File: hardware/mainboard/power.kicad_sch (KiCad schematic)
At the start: 18 parts, among them J1 Eurorack Power, U1 LD1117-3.3, U2 LM4040DBZ-10

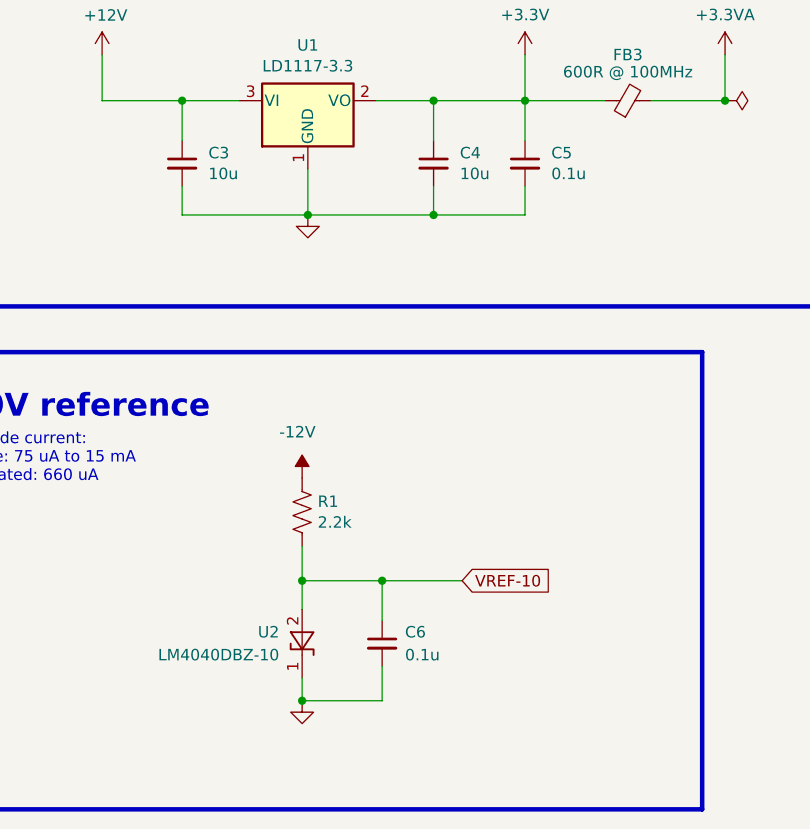
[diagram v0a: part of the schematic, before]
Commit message: Switch audio filter caps to 0603. Start auditing BOM
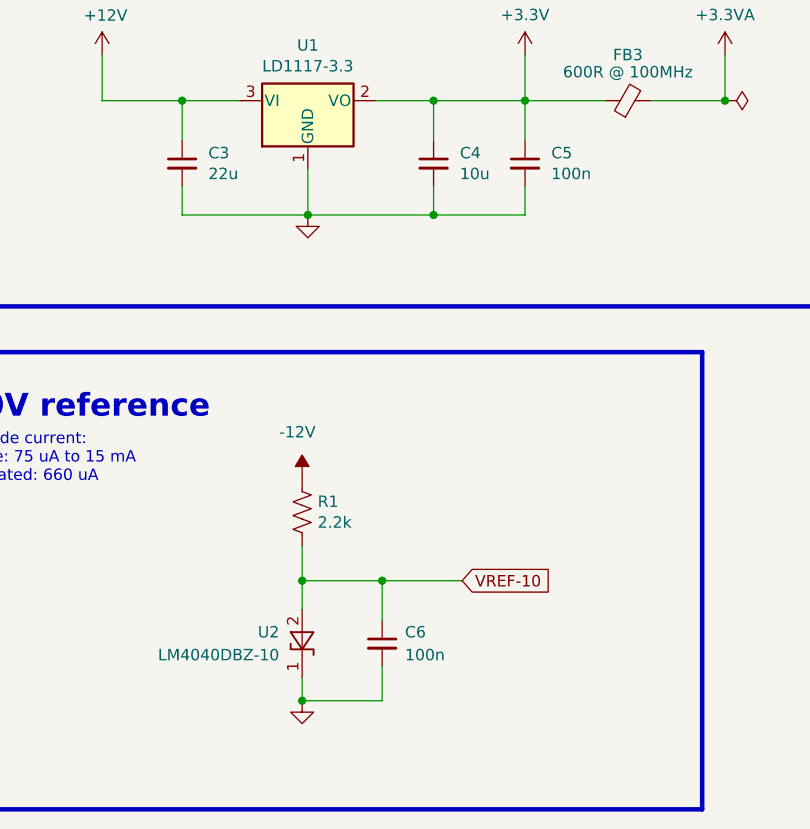
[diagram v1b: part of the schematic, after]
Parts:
- C1: Reqs power bypass, 16V+ -> Bulk capacitance, 16 V
- C2: Reqs power bypass, 16V+ -> Board bulk capacitance, 16 V
- C3: value 10u -> 22u; Reqs ESR 0.3-22 Ohms, 16v+ -> Linear regulator input filter, 16 V
- C4: footprint Capacitor_SMD:C_0805_2012Metric_Pad1.18x1.45mm_HandSolder -> Capacitor_SMD:C_0603_1608Metric_Pad1.08x0.95mm_HandSolder; Reqs (none) -> Linear regulator output filter, 10 V; mpn (none) -> CL10A106MP8NNNC
- C5, C6: value 0.1u -> 100n; Reqs bypass, 16v+ -> Bypass, 16 V; finalized yes -> (none); mpn MF-CAP-0603-0.1uF -> (none); mpn alt GCM188R91E104KA37D -> (none); mpn specs 10%, 25v -> (none)
- D1, D2: Reqs Schottky, 1A -> (none); finalized yes -> (none)
- FB1, FB2: Reqs >500mA DC current -> Power filter, 500mA DC current; finalized yes -> (none)
- FB3: Reqs >200mA DC current -> Analog power filter, 200mA DC current; finalized yes -> (none)
- R1: Reqs 1%, 60mW, vref current control -> -10V zener current control, 1%, 60 mW; mpn alt ERA-3AED222V -> (none); mpn specs 125mW, 1% -> (none)
- TP1, TP2, TP3: finalized yes -> n/a
- U1: finalized no -> (none); mpn AZ1117CD-3.3TRG1, LD1117DT33TR -> LD1117DT33TR, AZ1117CD-3.3TRG1
- U2: finalized yes -> (none)
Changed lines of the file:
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@@
       (effects (font (size 1.27 1.27)) hide)
     )
-    (property "finalized" "yes" (id 4) (at 80.645 41.275 0)
+    (property "finalized" "" (id 4) (at 80.645 41.275 0)
       (effects (font (size 1.27 1.27)) hide)
     )
@@
       (effects (font (size 1.27 1.27)) hide)
     )
-    (property "Reqs" "Schottky, 1A" (id 7) (at 80.645 41.275 0)
+    (property "Reqs" "" (id 7) (at 80.645 41.275 0)
       (effects (font (size 1.27 1.27)) hide)
     )
@@
       (effects (font (size 1.27 1.27)) hide)
     )
-    (property "finalized" "yes" (id 4) (at 80.645 37.465 0)
+    (property "finalized" "" (id 4) (at 80.645 37.465 0)
       (effects (font (size 1.27 1.27)) hide)
     )
@@
       (effects (font (size 1.27 1.27)) hide)
     )
-    (property "Reqs" "Schottky, 1A" (id 7) (at 80.645 37.465 0)
+    (property "Reqs" "" (id 7) (at 80.645 37.465 0)
       (effects (font (size 1.27 1.27)) hide)
     )
@@
       (effects (font (size 1.27 1.27)) hide)
     )
-    (property "finalized" "no" (id 4) (at 60.325 109.22 0)
-      (effects (font (size 1.27 1.27)) hide)
-    )
-    (property "mpn" "AZ1117CD-3.3TRG1, LD1117DT33TR" (id 5) (at 60.325 109.22 0)
+    (property "finalized" "" (id 4) (at 60.325 109.22 0)
+      (effects (font (size 1.27 1.27)) hide)
+    )
+    (property "mpn" "LD1117DT33TR, AZ1117CD-3.3TRG1" (id 5) (at 60.325 109.22 0)
       (effects (font (size 1.27 1.27)) hide)
     )
@@
       (effects (font (size 1.27 1.27)) (justify left))
     )
-    (property "Value" "10u" (id 1) (at 49.276 117.348 0)
+    (property "Value" "22u" (id 1) (at 49.276 117.348 0)
       (effects (font (size 1.27 1.27)) (justify left))
     )
@@
       (effects (font (size 1.27 1.27)) hide)
     )
-    (property "Reqs" "ESR 0.3-22 Ohms, 16v+" (id 6) (at 46.355 116.205 0)
+    (property "Reqs" "Linear regulator input filter, 16 V" (id 6) (at 46.355 116.205 0)
       (effects (font (size 1.27 1.27)) hide)
     )
@@
       (effects (font (size 1.27 1.27)) (justify left))
     )
-    (property "Footprint" "Capacitor_SMD:C_0805_2012Metric_Pad1.18x1.45mm_HandSolder" (id 2) (at 74.295 116.205 0)
+    (property "Footprint" "Capacitor_SMD:C_0603_1608Metric_Pad1.08x0.95mm_HandSolder" (id 2) (at 74.295 116.205 0)
       (effects (font (size 1.27 1.27)) hide)
     )
@@
       (effects (font (size 1.27 1.27)) hide)
     )
-    (property "Reqs" "" (id 4) (at 74.295 116.205 0)
-      (effects (font (size 1.27 1.27)) hide)
-    )
-    (property "mpn" "" (id 5) (at 74.295 116.205 0)
+    (property "Reqs" "Linear regulator output filter, 10 V" (id 4) (at 74.295 116.205 0)
+      (effects (font (size 1.27 1.27)) hide)
+    )
+    (property "mpn" "CL10A106MP8NNNC" (id 5) (at 74.295 116.205 0)
       (effects (font (size 1.27 1.27)) hide)
     )
@@
       (effects (font (size 1.27 1.27)) (justify left))
     )
-    (property "Value" "0.1u" (id 1) (at 87.376 117.348 0)
+    (property "Value" "100n" (id 1) (at 87.376 117.348 0)
       (effects (font (size 1.27 1.27)) (justify left))
     )
@@
       (effects (font (size 1.27 1.27)) hide)
     )
-    (property "finalized" "yes" (id 4) (at 84.455 116.205 0)
-      (effects (font (size 1.27 1.27)) hide)
-    )
-    (property "mpn" "MF-CAP-0603-0.1uF" (id 5) (at 84.455 116.205 0)
-      (effects (font (size 1.27 1.27)) hide)
-    )
-    (property "mpn specs" "10%, 25v" (id 6) (at 84.455 116.205 0)
-      (effects (font (size 1.27 1.27)) hide)
-    )
-    (property "mpn alt" "GCM188R91E104KA37D" (id 7) (at 84.455 116.205 0)
-      (effects (font (size 1.27 1.27)) hide)
-    )
-    (property "Reqs" "bypass, 16v+" (id 8) (at 84.455 116.205 0)
+    (property "finalized" "" (id 4) (at 84.455 116.205 0)
+      (effects (font (size 1.27 1.27)) hide)
+    )
+    (property "mpn" "" (id 5) (at 84.455 116.205 0)
+      (effects (font (size 1.27 1.27)) hide)
+    )
+    (property "mpn specs" "" (id 6) (at 84.455 116.205 0)
+      (effects (font (size 1.27 1.27)) hide)
+    )
+    (property "mpn alt" "" (id 7) (at 84.455 116.205 0)
+      (effects (font (size 1.27 1.27)) hide)
+    )
+    (property "Reqs" "Bypass, 16 V" (id 8) (at 84.455 116.205 0)
       (effects (font (size 1.27 1.27)) hide)
     )
@@
       (effects (font (size 1.27 1.27)) hide)
     )
-    (property "finalized" "yes" (id 5) (at 95.885 109.22 0)
+    (property "finalized" "" (id 5) (at 95.885 109.22 0)
       (effects (font (size 1.27 1.27)) hide)
     )
@@
       (effects (font (size 1.27 1.27)) hide)
     )
-    (property "Reqs" ">200mA DC current" (id 7) (at 95.885 109.22 0)
+    (property "Reqs" "Analog power filter, 200mA DC current" (id 7) (at 95.885 109.22 0)
       (effects (font (size 1.27 1.27)) hide)
     )
@@
       (effects (font (size 1.27 1.27)) hide)
     )
-    (property "finalized" "yes" (id 5) (at 62.23 41.275 0)
+    (property "finalized" "" (id 5) (at 62.23 41.275 0)
       (effects (font (size 1.27 1.27)) hide)
     )
@@
       (effects (font (size 1.27 1.27)) hide)
     )
-    (property "Reqs" ">500mA DC current" (id 7) (at 62.23 41.275 0)
+    (property "Reqs" "Power filter, 500mA DC current" (id 7) (at 62.23 41.275 0)
       (effects (font (size 1.27 1.27)) hide)
     )
@@
       (effects (font (size 1.27 1.27)) hide)
     )
-    (property "finalized" "yes" (id 5) (at 62.23 37.465 0)
+    (property "finalized" "" (id 5) (at 62.23 37.465 0)
       (effects (font (size 1.27 1.27)) hide)
     )
@@
       (effects (font (size 1.27 1.27)) hide)
     )
-    (property "Reqs" ">500mA DC current" (id 7) (at 62.23 37.465 0)
+    (property "Reqs" "Power filter, 500mA DC current" (id 7) (at 62.23 37.465 0)
       (effects (font (size 1.27 1.27)) hide)
     )
@@
       (effects (font (size 1.27 1.27) italic) hide)
     )
-    (property "finalized" "yes" (id 4) (at 59.69 169.545 0)
+    (property "finalized" "" (id 4) (at 59.69 169.545 0)
       (effects (font (size 1.27 1.27)) hide)
     )
@@
       (effects (font (size 1.27 1.27)) hide)
     )
-    (property "Reqs" "1%, 60mW, vref current control" (id 6) (at 59.69 154.94 0)
-      (effects (font (size 1.27 1.27)) hide)
-    )
-    (property "mpn specs" "125mW,  1%" (id 7) (at 59.69 154.94 0)
-      (effects (font (size 1.27 1.27)) hide)
-    )
-    (property "mpn alt" "ERA-3AED222V" (id 8) (at 59.69 154.94 0)
+    (property "Reqs" "-10V zener current control, 1%, 60 mW" (id 6) (at 59.69 154.94 0)
+      (effects (font (size 1.27 1.27)) hide)
+    )
+    (property "mpn specs" "" (id 7) (at 59.69 154.94 0)
+      (effects (font (size 1.27 1.27)) hide)
+    )
+    (property "mpn alt" "" (id 8) (at 59.69 154.94 0)
       (effects (font (size 1.27 1.27)) hide)
     )
@@
       (effects (font (size 1.27 1.27)) (justify left))
     )
-    (property "Value" "0.1u" (id 1) (at 71.12 170.815 0)
+    (property "Value" "100n" (id 1) (at 71.12 170.815 0)
       (effects (font (size 1.27 1.27)) (justify left))
     )
@@
       (effects (font (size 1.27 1.27)) hide)
     )
-    (property "finalized" "yes" (id 4) (at 68.58 169.545 0)
-      (effects (font (size 1.27 1.27)) hide)
-    )
-    (property "mpn" "MF-CAP-0603-0.1uF" (id 5) (at 68.58 169.545 0)
-      (effects (font (size 1.27 1.27)) hide)
-    )
-    (property "mpn specs" "10%, 25v" (id 6) (at 68.58 169.545 0)
-      (effects (font (size 1.27 1.27)) hide)
-    )
-    (property "mpn alt" "GCM188R91E104KA37D" (id 7) (at 68.58 169.545 0)
-      (effects (font (size 1.27 1.27)) hide)
-    )
-    (property "Reqs" "bypass, 16v+" (id 8) (at 68.58 169.545 0)
+    (property "finalized" "" (id 4) (at 68.58 169.545 0)
+      (effects (font (size 1.27 1.27)) hide)
+    )
+    (property "mpn" "" (id 5) (at 68.58 169.545 0)
+      (effects (font (size 1.27 1.27)) hide)
+    )
+    (property "mpn specs" "" (id 6) (at 68.58 169.545 0)
+      (effects (font (size 1.27 1.27)) hide)
+    )
+    (property "mpn alt" "" (id 7) (at 68.58 169.545 0)
+      (effects (font (size 1.27 1.27)) hide)
+    )
+    (property "Reqs" "Bypass, 16 V" (id 8) (at 68.58 169.545 0)
       (effects (font (size 1.27 1.27)) hide)
     )
@@
       (effects (font (size 1.27 1.27)) hide)
     )
-    (property "Reqs" "power bypass, 16V+" (id 7) (at 88.265 52.07 0)
+    (property "Reqs" "Bulk capacitance, 16 V" (id 7) (at 88.265 52.07 0)
       (effects (font (size 1.27 1.27)) hide)
     )
@@
       (effects (font (size 1.27 1.27)) hide)
     )
-    (property "finalized" "yes" (id 5) (at 234.95 146.685 0)
+    (property "finalized" "n/a" (id 5) (at 234.95 146.685 0)
       (effects (font (size 1.27 1.27)) hide)
     )
@@
       (effects (font (size 1.27 1.27)) hide)
     )
-    (property "finalized" "yes" (id 5) (at 234.95 135.255 0)
+    (property "finalized" "n/a" (id 5) (at 234.95 135.255 0)
       (effects (font (size 1.27 1.27)) hide)
     )
@@
       (effects (font (size 1.27 1.27)) hide)
     )
-    (property "Reqs" "power bypass, 16V+" (id 7) (at 99.06 52.07 0)
+    (property "Reqs" "Board bulk capacitance, 16 V" (id 7) (at 99.06 52.07 0)
       (effects (font (size 1.27 1.27)) hide)
     )
@@
       (effects (font (size 1.27 1.27)) hide)
     )
-    (property "finalized" "yes" (id 5) (at 234.95 140.97 0)
-      (effects (font (size 1.27 1.27)) hide)
-    )
+    (property "finalized" "n/a" (id 5) (at 234.95 140.97 0)
+      (effects (font (size 1.27 1.27)) hide)
+    )

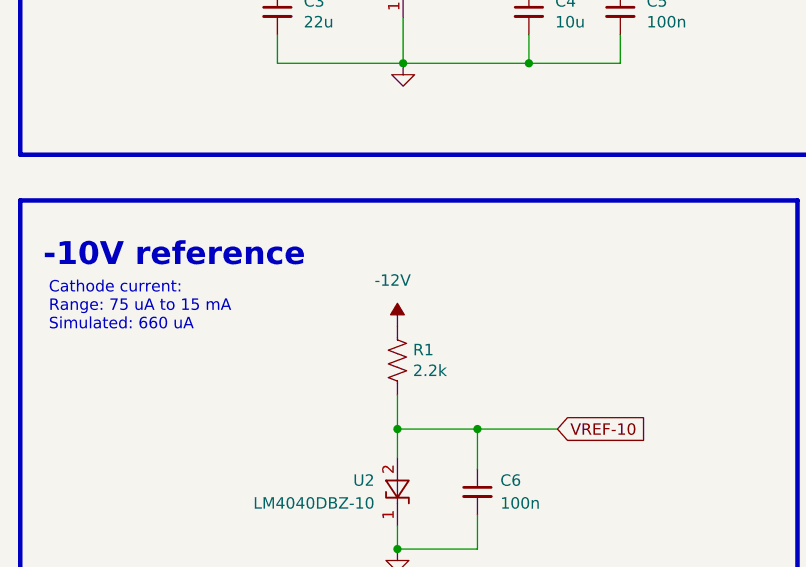
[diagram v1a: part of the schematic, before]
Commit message: Audit BOM, replace some parts with alts
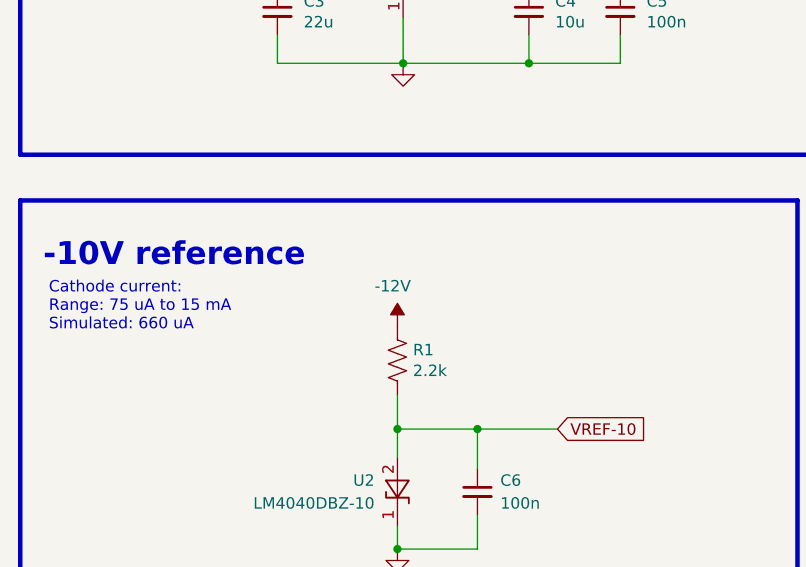
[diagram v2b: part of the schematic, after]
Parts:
- C1, C2, C3: finalized (none) -> yes; mpn (none) -> CL21A226MAYNNNE
- C4, FB1, FB2, FB3, U2: finalized (none) -> yes
- C5, C6: finalized (none) -> yes; macrofab_mpn (none) -> MF-CAP-0402-0.1uF; mpn (none) -> CL05B104KO5NNNC
- D1, D2: finalized (none) -> yes; mpn B0520LWQ-7-F -> PMEG2005EGWJ, PMEG3005EGWX
- J1: finalized (none) -> yes; mpn 302-S101 -> 4UCONN 20253, On-shore 302-S101
- R1: Reqs -10V zener current control, 1%, 60 mW -> -10V zener current control, 1%, 100 mW, thick film; macrofab_mpn (none) -> MF-RES-0402-2K
- U1: finalized (none) -> needs testing
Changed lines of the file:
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@@
       (effects (font (size 1.27 1.27)) hide)
     )
-    (property "finalized" "" (id 4) (at 80.645 41.275 0)
-      (effects (font (size 1.27 1.27)) hide)
-    )
-    (property "mpn" "B0520LWQ-7-F" (id 5) (at 80.645 41.275 0)
+    (property "finalized" "yes" (id 4) (at 80.645 41.275 0)
+      (effects (font (size 1.27 1.27)) hide)
+    )
+    (property "mpn" "PMEG2005EGWJ, PMEG3005EGWX" (id 5) (at 80.645 41.275 0)
       (effects (font (size 1.27 1.27)) hide)
     )
@@
       (effects (font (size 1.27 1.27)) hide)
     )
-    (property "finalized" "" (id 4) (at 80.645 37.465 0)
-      (effects (font (size 1.27 1.27)) hide)
-    )
-    (property "mpn" "B0520LWQ-7-F" (id 5) (at 80.645 37.465 0)
+    (property "finalized" "yes" (id 4) (at 80.645 37.465 0)
+      (effects (font (size 1.27 1.27)) hide)
+    )
+    (property "mpn" "PMEG2005EGWJ, PMEG3005EGWX" (id 5) (at 80.645 37.465 0)
       (effects (font (size 1.27 1.27)) hide)
     )
@@
       (effects (font (size 1.27 1.27)) hide)
     )
-    (property "finalized" "" (id 4) (at 60.325 109.22 0)
+    (property "finalized" "needs testing" (id 4) (at 60.325 109.22 0)
       (effects (font (size 1.27 1.27)) hide)
     )
@@
       (effects (font (size 1.27 1.27)) hide)
     )
-    (property "mpn" "" (id 4) (at 46.355 116.205 0)
-      (effects (font (size 1.27 1.27)) hide)
-    )
-    (property "finalized" "" (id 5) (at 46.355 116.205 0)
+    (property "mpn" "CL21A226MAYNNNE" (id 4) (at 46.355 116.205 0)
+      (effects (font (size 1.27 1.27)) hide)
+    )
+    (property "finalized" "yes" (id 5) (at 46.355 116.205 0)
       (effects (font (size 1.27 1.27)) hide)
     )
@@
       (effects (font (size 1.27 1.27)) hide)
     )
-    (property "finalized" "" (id 6) (at 74.295 116.205 0)
+    (property "finalized" "yes" (id 6) (at 74.295 116.205 0)
       (effects (font (size 1.27 1.27)) hide)
     )
@@
       (effects (font (size 1.27 1.27)) hide)
     )
-    (property "finalized" "" (id 4) (at 84.455 116.205 0)
-      (effects (font (size 1.27 1.27)) hide)
-    )
-    (property "mpn" "" (id 5) (at 84.455 116.205 0)
+    (property "finalized" "yes" (id 4) (at 84.455 116.205 0)
+      (effects (font (size 1.27 1.27)) hide)
+    )
+    (property "mpn" "CL05B104KO5NNNC" (id 5) (at 84.455 116.205 0)
       (effects (font (size 1.27 1.27)) hide)
     )
@@
     )
     (property "Reqs" "Bypass, 16 V" (id 8) (at 84.455 116.205 0)
+      (effects (font (size 1.27 1.27)) hide)
+    )
+    (property "macrofab_mpn" "MF-CAP-0402-0.1uF" (id 9) (at 84.455 116.205 0)
       (effects (font (size 1.27 1.27)) hide)
     )
@@
       (effects (font (size 1.27 1.27)) hide)
     )
-    (property "finalized" "" (id 5) (at 95.885 109.22 0)
+    (property "finalized" "yes" (id 5) (at 95.885 109.22 0)
       (effects (font (size 1.27 1.27)) hide)
     )
@@
       (effects (font (size 1.27 1.27)) hide)
     )
-    (property "finalized" "" (id 5) (at 62.23 41.275 0)
+    (property "finalized" "yes" (id 5) (at 62.23 41.275 0)
       (effects (font (size 1.27 1.27)) hide)
     )
@@
       (effects (font (size 1.27 1.27)) hide)
     )
-    (property "finalized" "" (id 5) (at 62.23 37.465 0)
+    (property "finalized" "yes" (id 5) (at 62.23 37.465 0)
       (effects (font (size 1.27 1.27)) hide)
     )
@@
       (effects (font (size 1.27 1.27) italic) hide)
     )
-    (property "finalized" "" (id 4) (at 59.69 169.545 0)
+    (property "finalized" "yes" (id 4) (at 59.69 169.545 0)
       (effects (font (size 1.27 1.27)) hide)
     )
@@
       (effects (font (size 1.27 1.27)) hide)
     )
-    (property "Value" "-12V" (id 1) (at 57.15 146.05 0)
+    (property "Value" "-12V" (id 1) (at 57.15 146.685 0)
       (effects (font (size 1.27 1.27)) (justify left))
     )
@@
       (effects (font (size 1.27 1.27)) hide)
     )
-    (property "Reqs" "-10V zener current control, 1%, 60 mW" (id 6) (at 59.69 154.94 0)
+    (property "Reqs" "-10V zener current control, 1%, 100 mW, thick film" (id 6) (at 59.69 154.94 0)
       (effects (font (size 1.27 1.27)) hide)
     )
@@
       (effects (font (size 1.27 1.27)) hide)
     )
+    (property "macrofab_mpn" "MF-RES-0402-2K" (id 9) (at 59.69 154.94 0)
+      (effects (font (size 1.27 1.27)) hide)
+    )
     (pin "1")
     (pin "2")
@@
       (effects (font (size 1.27 1.27)) hide)
     )
-    (property "finalized" "" (id 4) (at 68.58 169.545 0)
-      (effects (font (size 1.27 1.27)) hide)
-    )
-    (property "mpn" "" (id 5) (at 68.58 169.545 0)
+    (property "finalized" "yes" (id 4) (at 68.58 169.545 0)
+      (effects (font (size 1.27 1.27)) hide)
+    )
+    (property "mpn" "CL05B104KO5NNNC" (id 5) (at 68.58 169.545 0)
       (effects (font (size 1.27 1.27)) hide)
     )
@@
       (effects (font (size 1.27 1.27)) hide)
     )
+    (property "macrofab_mpn" "MF-CAP-0402-0.1uF" (id 9) (at 68.58 169.545 0)
+      (effects (font (size 1.27 1.27)) hide)
+    )
     (pin "1")
     (pin "2")
@@
       (effects (font (size 1.27 1.27)) hide)
     )
-    (property "mpn" "" (id 4) (at 88.265 52.07 0)
-      (effects (font (size 1.27 1.27)) hide)
-    )
-    (property "finalized" "" (id 5) (at 88.265 52.07 0)
+    (property "mpn" "CL21A226MAYNNNE" (id 4) (at 88.265 52.07 0)
+      (effects (font (size 1.27 1.27)) hide)
+    )
+    (property "finalized" "yes" (id 5) (at 88.265 52.07 0)
       (effects (font (size 1.27 1.27)) hide)
     )
@@
       (effects (font (size 1.27 1.27)) hide)
     )
-    (property "mpn" "302-S101" (id 4) (at 39.37 27.305 0)
+    (property "mpn" "4UCONN 20253, On-shore 302-S101" (id 4) (at 39.37 27.305 0)
+      (effects (font (size 1.27 1.27)) hide)
+    )
+    (property "finalized" "yes" (id 5) (at 39.37 41.275 0)
       (effects (font (size 1.27 1.27)) hide)
     )
@@
       (effects (font (size 1.27 1.27)) hide)
     )
-    (property "mpn" "" (id 4) (at 99.06 52.07 0)
-      (effects (font (size 1.27 1.27)) hide)
-    )
-    (property "finalized" "" (id 5) (at 99.06 52.07 0)
-      (effects (font (size 1.27 1.27)) hide)
-    )
+    (property "mpn" "CL21A226MAYNNNE" (id 4) (at 99.06 52.07 0)
+      (effects (font (size 1.27 1.27)) hide)
+    )
+    (property "finalized" "yes" (id 5) (at 99.06 52.07 0)
+      (effects (font (size 1.27 1.27)) hide)
+    )
